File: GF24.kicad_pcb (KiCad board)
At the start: 4 copper layers, 82 x 40 mm, 69 parts, among them J1 Conn_ARM_SWD_TagConnect_TC2030, J2 USB4110GFA, J3 S2B-PH-SM4-TB, J4 0533980671, J5 0533980671, Q1 3904, Q2 DMN3731U-7, Q3 DMN3731U-7, Q4 DMP2004K-7, Q5 DMP2004K-7, Q6 DMP2004K-7, SW2 BOOT, U1 STM32F031C4T6, U2 SAM-M10Q, U3 TPS745, U4 LTC1733, U5 ST-025BH, U6 M24C02-WMN6TP, Y1 CS06465-32M

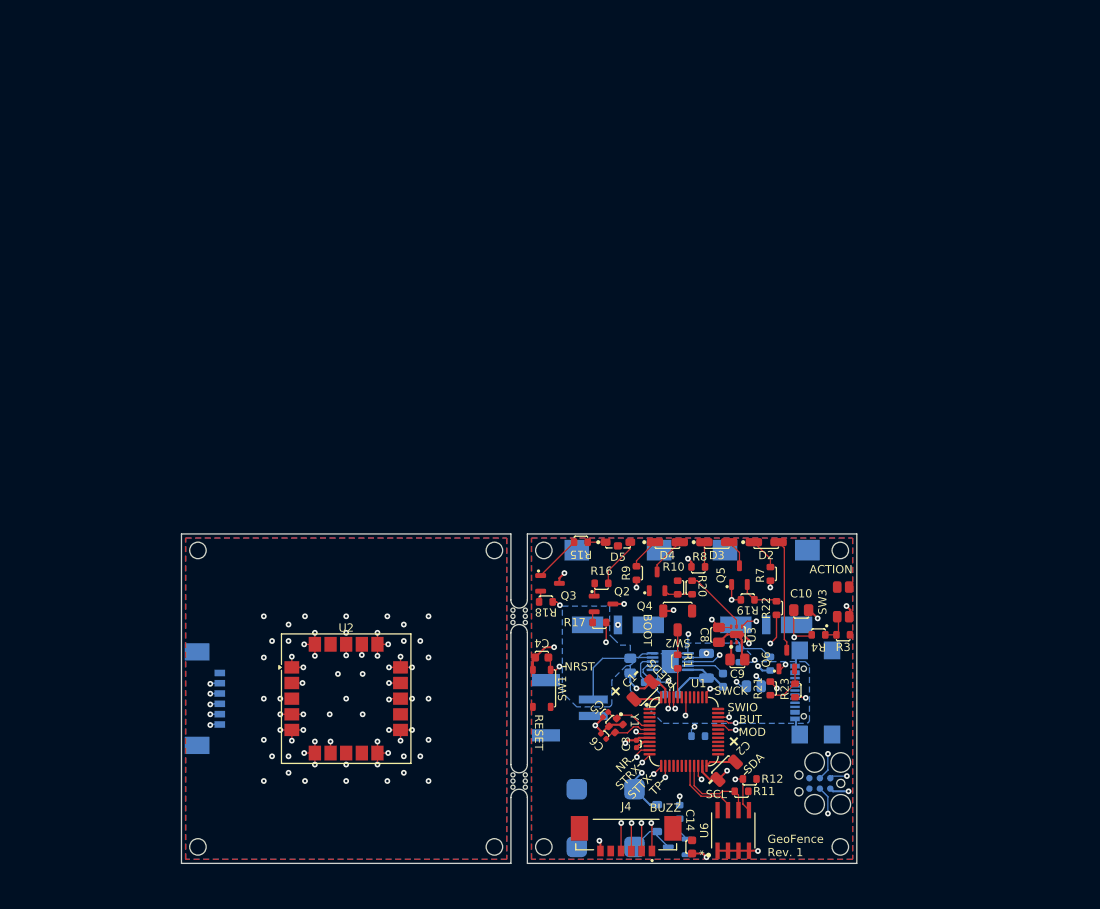
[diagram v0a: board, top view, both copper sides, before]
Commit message: need to finish placement but this is an almost completed R2
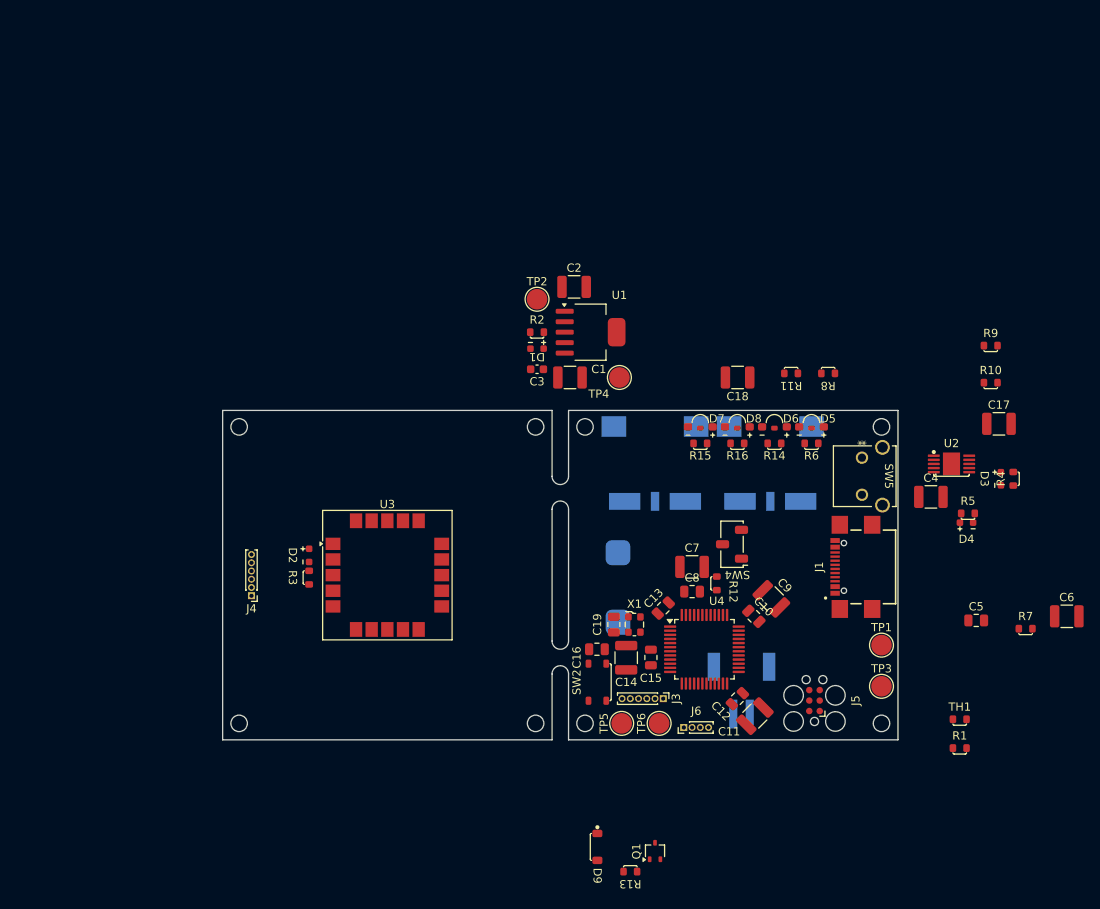
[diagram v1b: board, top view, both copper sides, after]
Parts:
- removed G***: LOGO, MB-Initials:initials-5mm
- removed Q2, Q3: DMN3731U-7, MB-SOT:SOT-23-3
- removed Q4, Q5, Q6: DMP2004K-7, MB-SOT:SOT-23-3
- removed R17, R18, R20, R22, R23: 1k, MB-Generic:R0603_medium
- removed R19, R21: 10k, MB-Generic:R0603_medium
- removed U5: ST-025BH, MB-Buzzer:ST-025BH_SOB
- removed U6: M24C02-WMN6TP, MB-SOIC:SO-8_STM
- removed Y1: CS06465-32M, MB-Crystal:CS06465-32M
- removed mouse-bite-2mm-slot (x2): VAL**, MB-Tab:mouse-bite-2mm-slot
- added BZ1: SMTB-0927-TW-R, MB-Buzzer:SMTB-0927-TW-R, B.Cu at (123.0, 96.5)
- added C16: 100nf, Capacitor_SMD:C_0805_2012Metric, F.Cu at (120.4, 104.0)
- added C17: 1uF, Capacitor_SMD:C_1210_3225Metric, F.Cu at (169.3, 76.6)
- added C18: 1uF, Capacitor_SMD:C_1210_3225Metric, F.Cu at (137.5, 71.0)
- added C19: 100nf, Capacitor_SMD:C_0805_2012Metric, F.Cu at (122.5, 101.0)
- added C7: 10uF, Capacitor_SMD:C_1210_3225Metric, F.Cu at (132.0, 94.0)
- added D6: LED, MB-Opto:WE-1204-Mono-Side, F.Cu at (142.0, 77.0)
- added D7: LED, MB-Opto:WE-1204-Mono-Side, F.Cu at (133.0, 77.0)
- added D8: LED, MB-Opto:WE-1204-Mono-Side, F.Cu at (137.5, 77.0)
- added D9: D, MB-SOD:SOD-123-2, F.Cu at (120.5, 128.0)
- added J6: Conn_01x04_Pin, Connector_PinHeader_1.00mm:PinHeader_1x04_P1.00mm_Vertical, F.Cu at (131.0, 113.5)
- added TP1: TestPoint, TestPoint:TestPoint_Pad_D2.5mm, F.Cu at (155.0, 103.5)
- added TP2: TestPoint, TestPoint:TestPoint_Pad_D2.5mm, F.Cu at (113.2, 61.5)
- added TP3: TestPoint, TestPoint:TestPoint_Pad_D2.5mm, F.Cu at (155.0, 108.5)
- added TP4: TestPoint, TestPoint:TestPoint_Pad_D2.5mm, F.Cu at (123.2, 71.0)
- added TP5: TestPoint, TestPoint:TestPoint_Pad_D2.5mm, F.Cu at (123.5, 113.0)
- added TP6: TestPoint, TestPoint:TestPoint_Pad_D2.5mm, F.Cu at (128.0, 113.0)
- added X1: ECS-2520MV-160-CN, Oscillator:Oscillator_SMD_ECS_2520MV-xxx-xx-4Pin_2.5x2.0mm, F.Cu at (125.0, 101.0)
- C1, C2: value 4.7uF -> 1uF; footprint MB-Generic:C1206_medium -> Capacitor_SMD:C_1210_3225Metric
- C10, C8: value 1uF -> 100nf; footprint MB-Generic:C0805_medium -> Capacitor_SMD:C_0805_2012Metric
- C11: value 4.7uF -> 10uF; footprint MB-Generic:C1206_medium -> Capacitor_SMD:C_1210_3225Metric; moved to F.Cu
- C12: value 0.1uF -> 100nf; footprint MB-Generic:C0603_medium -> Capacitor_SMD:C_0805_2012Metric; moved to F.Cu
- C13, C15: value 1uF -> 100nf; footprint MB-Generic:C0805_medium -> Capacitor_SMD:C_0805_2012Metric; moved to F.Cu
- C14: value 0.1uF -> 1uF; footprint MB-Generic:C0603_medium -> Capacitor_SMD:C_1210_3225Metric
- C3: footprint MB-Generic:C0402_medium -> Capacitor_SMD:C_0603_1608Metric
- C4: value 0.1uF -> 4.7uF; footprint MB-Generic:C0603_medium -> Capacitor_SMD:C_1210_3225Metric
- C5: value 10pF -> 100nf; footprint MB-Generic:C0402_medium -> Capacitor_SMD:C_0805_2012Metric
- C6: value 10pF -> 1uF; footprint MB-Generic:C0402_medium -> Capacitor_SMD:C_1210_3225Metric
- C9: value 1uF -> 10uF; footprint MB-Generic:C0805_medium -> Capacitor_SMD:C_1210_3225Metric
- D1: value D -> LED; footprint MB-SOD:SOD-123-2 -> MB-Opto:WE-0603-Mono-Chip-Advance; moved to F.Cu
- D2, D3, D4: footprint MB-Opto:Kingbright-APDA3020 -> MB-Opto:WE-0603-Mono-Chip-Advance
- D5: value APBDA3020SURKCGKC-GX -> LED; footprint MB-Opto:Kingbright-APBDA3020 -> MB-Opto:WE-1204-Mono-Side
- J1: value Conn_ARM_SWD_TagConnect_TC2030 -> USB4110GFA; footprint MB-Conn:Tag-Connect_TC2030-IDC-FP_2x03_P1.27mm_Vertical -> MB-Conn:GCT_USB4110GFA; moved to F.Cu
- J2: value USB4110GFA -> S2B-PH-SM4-TB; footprint MB-Conn:GCT_USB4110GFA -> MB-Conn:JST_S2B-PH-SM4-TB
- J3: value S2B-PH-SM4-TB -> Conn_01x06_Pin; footprint MB-Conn:JST_S2B-PH-SM4-TB -> Connector_PinHeader_1.00mm:PinHeader_1x06_P1.00mm_Vertical; moved to F.Cu
- J4: value 0533980671 -> Conn_01x06_Pin; footprint MB-Conn:MOLEX_0533980671 -> Connector_PinHeader_1.00mm:PinHeader_1x06_P1.00mm_Vertical
- J5: value 0533980671 -> Conn_ARM_SWD_TagConnect_TC2030; footprint MB-Conn:MOLEX_0533980671 -> Connector:Tag-Connect_TC2030-IDC-FP_2x03_P1.27mm_Vertical; moved to F.Cu
- Q1: footprint MB-SOT:SOT-23-3 -> Package_TO_SOT_SMD:SOT-323_SC-70; moved to F.Cu
- R1: value 10k -> 4.12k
- R11, R12: value 4.7k -> 10k
- R13: value 10k -> 180; moved to F.Cu
- R14: value 1k -> 2; moved to F.Cu
- R15, R16: value 47 -> 2
- R2: value 180 -> 260; moved to F.Cu
- R3: value 1k -> 260
- R4: value 10k -> 1k
- R5: value 1.5k -> 1k; moved to F.Cu
- R6: value 4.12k -> 1k; moved to F.Cu
- R7: value 127 -> 1.5k
- R8: value 127 -> 1k
- R9: value 51 -> 1k
- SW1: footprint MB-SW:PTS815SJM250SMTRLFS -> MB-SW:SW_500ASSP1SM6QE; moved to B.Cu
- SW2: value BOOT -> ~; footprint MB-SW:CJS-1200TA -> MB-SW:PTS815SJM250SMTRLFS
- SW3: footprint MB-SW:TL1016AAF160QG -> MB-SW:SW_500ASSP1SM6QE; moved to B.Cu
- SW4: value ~ -> BOOT; footprint MB-SW:SW_500ASSP1SM6QE -> Button_Switch_SMD:Nidec_Copal_CAS-120A; moved to F.Cu
- SW5: value ~ -> 1-1825027-7; footprint MB-SW:SW_500ASSP1SM6QE -> MB-SW:SW2_1825027-F_TEC; moved to F.Cu
- TH1: moved to F.Cu
- U1: value STM32F031C4T6 -> TPS79533DCQR; footprint MB-STM:LQFP-48_7x7mm_P0.5mm -> Package_TO_SOT_SMD:SOT-223-6
- U2: value SAM-M10Q -> LTC1733; footprint MB-GNSS:SAM-M10Q -> MB-MSOP:10-MSOP-TE
- U3: value TPS745 -> SAM-M10Q; footprint MB-DFN:6-WDFN -> MB-GNSS:SAM-M10Q
- U4: value LTC1733 -> STM32F102C8Tx; footprint MB-MSOP:10-MSOP-TE -> Package_QFP:LQFP-48_7x7mm_P0.5mm; moved to F.Cu
- moved U2 78.8 mm to (163.5, 81.5)
- moved J5 72.9 mm to (146.9, 110.2)
- moved R3 65.2 mm to (85.5, 95.3), turned to -90 degrees
- moved C2 61.6 mm to (117.7, 60.0), turned to 0 degrees
- moved R2 60.8 mm to (113.2, 65.5), turned to 0 degrees
- moved D1 58.8 mm to (113.2, 67.5), turned to 180 degrees
- moved C6 58.1 mm to (177.5, 100.0), turned to 0 degrees
- moved D2 55.5 mm to (85.5, 92.6), turned to -90 degrees
- moved J4 54.7 mm to (78.5, 97.5)
- moved R9 51.1 mm to (168.3, 67.1), turned to 0 degrees
- moved C4 51.1 mm to (161.0, 85.5), turned to 0 degrees
- moved R11 51.1 mm to (144.0, 70.5), turned to 180 degrees
- moved U1 49.8 mm to (119.7, 65.5)
- moved C3 47.1 mm to (113.2, 70.0), turned to 0 degrees
- moved C5 46.4 mm to (166.5, 100.5), turned to 0 degrees
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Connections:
- C10 pad 1: BUTTON -> +3V3
- C11 pad 1: VBUS -> +3V3
- C12 pad 1: /CH-TIMER -> +3V3
- C13 pad 1: BAT+ -> +3V3
- C15 pad 1: MODE -> +3V3
- C2 pad 1: +3V3 -> /REG_I
- C3 pad 1: +3V3 -> Net-(U1-NR)
- C4 pad 1: NRST -> Net-(D3-A)
- C5 pad 1: /OSC-IN -> /CH-TIMER
- C6 pad 1: /OSC-OUT -> Net-(U2-BAT)
- C8 pad 1: /REG_I -> +3V3
- D1 pad 1: +3V3 -> Net-(D1-K)
- D1 pad 2: /BUZZ- -> +3V3
- D2 pad 1: /CHRG_RES -> Net-(D2-K)
- D2 pad 2: /CHRG_QO -> GNSS-3V3
- D3 pad 1: /FAULT_RES -> Net-(D3-K)
- D3 pad 2: /FAULT_QO -> Net-(D3-A)
- D4 pad 1: /PG_RES -> Net-(D4-K)
- D4 pad 2: /PG_QO -> Net-(D3-A)
- D5 pad 1: /STATR_RES -> Net-(D5-K)
- D5 pad 2: +3V3 -> Net-(D3-A)
- J3 pad 2: BAT+ -> /GNSS-ST-TIMEPULSE
- J3 pad 3: unconnected-(J3-Pad3) -> /GNSS-ST-RX2
- J3 pad 4: unconnected-(J3-Pad4) -> /GNSS-ST-TX2
- J4 pad 1: /GNSS-ST-TIMEPULSE -> GNSS-GND
- J4 pad 2: /GNSS-ST-TX -> GNSS-TIMEPULSE
- J4 pad 3: /GNSS-ST-RX -> GNSS-TX
- J4 pad 4: /GNSS-ST-N-RESET -> GNSS-RX
- J4 pad 5: +3V3 -> GNSS-N-RESET
- J4 pad 6: GND -> GNSS-3V3
- J5 pad 1: GNSS-TIMEPULSE -> +3V3
- J5 pad 2: GNSS-TX -> /SWDIO
- J5 pad 3: GNSS-RX -> NRST
- J5 pad 4: GNSS-N-RESET -> /SWDCLK
- J5 pad 5: GNSS-3V3 -> GND
- J5 pad 6: GNSS-GND -> unconnected-(J5-SWO-Pad6)
- R1 pad 1: /BOOT0_RES -> /CH-TH-DIV
- R1 pad 2: /BOOT0 -> Net-(D3-A)
- R10 pad 1: /PG_QG -> /ACT-H
- R10 pad 2: +3V3 -> BUTTON
- R11 pad 1: I2C-SCL -> /MODE-H
- R11 pad 2: +3V3 -> MODE
- R12 pad 1: I2C-SDA -> /BOOT0_RES
- R12 pad 2: +3V3 -> Net-(U4-BOOT0)
- R13 pad 1: /MODE-H -> /BUZZ-QB
- R13 pad 2: MODE -> BUZZER
- R14 pad 1: /MODE-H -> Net-(D6-K)
- R14 pad 2: +3V3 -> GND
- R15 pad 1: /STATR_RES -> Net-(D7-K)
- R15 pad 2: /STATR_QI -> GND
- R16 pad 1: /STATG_QI -> Net-(D8-K)
- R16 pad 2: /STATG_RES -> GND
- R2 pad 1: /BUZZ-QB -> Net-(D1-K)
- R2 pad 2: BUZZER -> GND
- R3 pad 1: /ACT-H -> Net-(D2-K)
- R3 pad 2: +3V3 -> GNSS-GND
- R4 pad 1: /ACT-H -> Net-(D3-K)
- R4 pad 2: BUTTON -> NACPR
- R5 pad 1: GND -> Net-(D4-K)
- R5 pad 2: /CH-PROG -> NFAULT
- R6 pad 1: /CH-TH-DIV -> Net-(D5-K)
- R6 pad 2: VBUS -> NCHRG
- R7 pad 2: /CHRG_RES -> /CH-PROG
- R8 pad 1: GND -> /MODE-H
- R8 pad 2: /FAULT_RES -> +3V3
- R9 pad 1: GND -> /ACT-H
- R9 pad 2: /PG_RES -> +3V3
- SW1 pad 1: unconnected-(SW1-Pad1) -> BAT+
- SW1 pad 2: GND -> /REG_I
- SW1 pad 4: NRST -> unconnected-(SW1-NC-Pad4)
- SW2 pad 1: +3V3 -> unconnected-(SW2-Pad1)
- SW2 pad 2: /BOOT0_RES -> GND
- SW2 pad 3: GND -> unconnected-(SW2-Pad3)
- SW3 pad 1: /ACT-H -> /MODE-H
- SW3 pad 2: unconnected-(SW3-Pad2) -> GND
- SW3 pad 3: GND -> unconnected-(SW3-Pad3)
- SW4 pad 1: BAT+ -> +3V3
- SW4 pad 2: /REG_I -> /BOOT0_RES
- SW4 pad 3: unconnected-(SW4-Pad3) -> GND
- SW5 pad 1: /MODE-H -> /ACT-H
- U1 pad 1: +3V3 -> /REG_I
- U1 pad 2: unconnected-(U1-PC13-Pad2) -> /REG_I
- U1 pad 3: unconnected-(U1-PC14-Pad3) -> GND
- U1 pad 4: unconnected-(U1-PC15-Pad4) -> +3V3
- U1 pad 5: /OSC-IN -> Net-(U1-NR)
- U1 pad 6: /OSC-OUT -> GND
- U2 pad 1: GNSS-GND -> NCHRG
- U2 pad 10: GNSS-GND -> NACPR
- U2 pad 11: GNSS-GND -> GND
- U2 pad 2: GNSS-3V3 -> Net-(D3-A)
- U2 pad 3: unconnected-(U2-V-BCKP-Pad3) -> NFAULT
- U2 pad 4: GNSS-GND -> /CH-TIMER
- U2 pad 5: GNSS-GND -> GND
- U2 pad 6: GNSS-GND -> /CH-TH-DIV
- U2 pad 7: GNSS-TIMEPULSE -> /CH-PROG
- U2 pad 8: unconnected-(U2-SAFEBOOT-N-Pad8) -> Net-(D3-A)
- U2 pad 9: unconnected-(U2-SDA-Pad9) -> Net-(U2-BAT)
- U3 pad 1: +3V3 -> GNSS-GND
- U3 pad 2: unconnected-(U3-NC-Pad2) -> GNSS-3V3
- U3 pad 3: GND -> unconnected-(U3-V-BCKP-Pad3)
- U3 pad 4: /REG_I -> GNSS-GND
- U3 pad 5: PG -> GNSS-GND
- U3 pad 6: /REG_I -> GNSS-GND
- U3 pad 7: GND -> GNSS-TIMEPULSE
- U4 pad 1: N-CHRG -> +3V3
- U4 pad 11: GND -> /GNSS-ST-N-RESET
- U4 pad 2: VBUS -> unconnected-(U4-PC13-Pad2)
- U4 pad 3: N-FAULT -> unconnected-(U4-PC14-Pad3)
- U4 pad 4: /CH-TIMER -> unconnected-(U4-PC15-Pad4)
- U4 pad 5: GND -> Net-(U4-PD0)
- U4 pad 6: /CH-TH-DIV -> unconnected-(U4-PD1-Pad6)
- U4 pad 7: /CH-PROG -> NRST
- U4 pad 8: VBUS -> GND
- U4 pad 9: BAT+ -> +3V3
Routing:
- net GND: track 72.7 -> 0.00 mm, vias 18 -> 0
- net NRST: track 48.6 -> 0.00 mm, vias 3 -> 0
- net GNSS-GND: track 34.2 -> 0.00 mm, vias 62 -> 0
- net GNSS-TX: track 25.5 -> 0.00 mm, vias 2 -> 0
- net GNSS-RX: track 25.4 -> 0.00 mm, vias 2 -> 0
- net /SWDCLK: track 22.4 -> 0.00 mm, vias 2 -> 0
- net N-CHRG: track 22.2 -> 0.00 mm, vias 2 -> 0
- net STATR: track 22.0 -> 0.00 mm, vias 2 -> 0
- net BUTTON: track 21.3 -> 0.00 mm, vias 2 -> 0
- net +3V3: track 21.1 -> 0.00 mm, vias 3 -> 0
- net GNSS-N-RESET: track 20.9 -> 0.00 mm, vias 2 -> 0
- net /SWDIO: track 20.7 -> 0.00 mm, vias 2 -> 0
- net VBUS: track 19.4 -> 0.00 mm, vias 4 -> 0
- net GNSS-TIMEPULSE: track 18.0 -> 0.00 mm, vias 2 -> 0
- net MODE: track 16.6 -> 0.00 mm, vias 3 -> 0
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- removed copper zone on F.Cu, net +3V3
- removed copper zone on In2.Cu, net /REG_I
- removed copper zone on B.Cu, net BAT+
- removed copper zone on B.Cu, net GND
- removed copper zone on In1.Cu, net GNSS-3V3
- removed copper zone on B.Cu, net GNSS-GND
- removed copper zone on F.Cu, net GNSS-GND
- removed copper zone on B.Cu, net VBUS
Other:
- board text removed: "+"
- board text removed: "-"
- board text removed: "ACTION"
- board text removed: "BAT+"
- board text removed: "BOOT"
- board text removed: "BUT"
- board text removed: "BUZZ"
- board text removed: "GeoFence Rev. 1"
- board text removed: "MOD"
- board text removed: "MODE"
- board text removed: "NR"
- board text removed: "NRST"
- board text removed: "PLEDS"
- board text removed: "PWR"
- board text removed: "RESET"
- board text removed: "SCL"
- board text removed: "SDA"
- board text removed: "STRX"
- board text removed: "STTX"
- board text removed: "SWCK"
- board text removed: "SWIO"
- board text removed: "TC"
- board text removed: "TP"
- board text removed: "VBUS"

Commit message: going to make some changes to the I/O
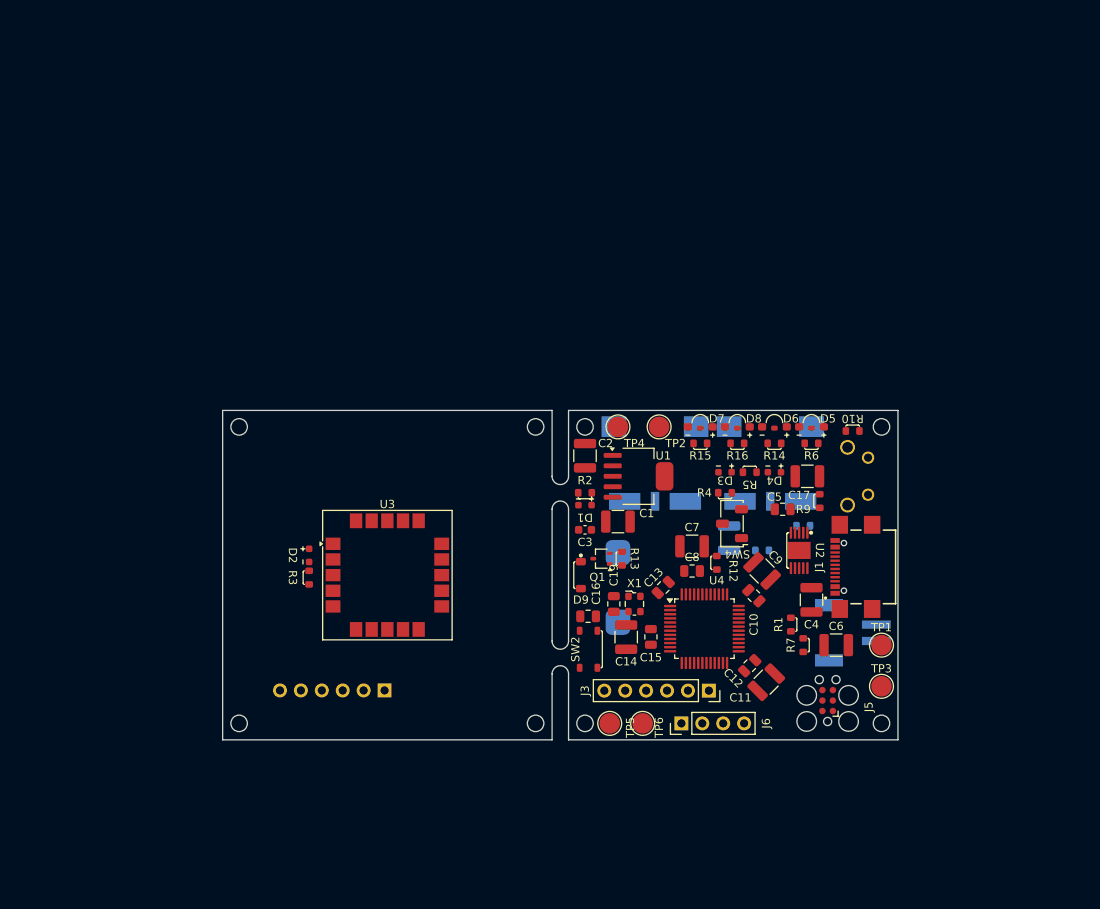
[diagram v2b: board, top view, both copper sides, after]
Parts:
- C18, R11, R8, SW5, TH1: moved to B.Cu
- J3: footprint Connector_PinHeader_1.00mm:PinHeader_1x06_P1.00mm_Vertical -> Connector_PinSocket_2.54mm:PinSocket_1x06_P2.54mm_Vertical
- J4: footprint Connector_PinHeader_1.00mm:PinHeader_1x06_P1.00mm_Vertical -> Connector_PinHeader_2.54mm:PinHeader_1x06_P2.54mm_Vertical; moved to B.Cu
- J6: footprint Connector_PinHeader_1.00mm:PinHeader_1x04_P1.00mm_Vertical -> Connector_PinHeader_2.54mm:PinHeader_1x04_P2.54mm_Vertical
- moved R13 38.0 mm to (123.5, 93.0), turned to -90 degrees
- moved Q1 36.1 mm to (121.0, 93.0), turned to 180 degrees
- moved R4 35.0 mm to (136.0, 85.0), turned to 0 degrees
- moved D3 33.5 mm to (136.0, 82.5), turned to 180 degrees
- moved D9 33.1 mm to (118.5, 95.0)
- moved TH1 31.6 mm to (140.5, 92.0), turned to 180 degrees
- moved C6 28.2 mm to (149.5, 103.5)
- moved R9 28.1 mm to (147.5, 86.0), turned to -90 degrees
- moved C5 27.1 mm to (143.0, 87.0), turned to 180 degrees
- moved R7 27.1 mm to (145.5, 103.5), turned to 90 degrees
- moved R5 27.0 mm to (139.0, 82.5), turned to 180 degrees
- moved R1 25.4 mm to (144.0, 101.0), turned to 90 degrees
- moved C17 24.1 mm to (146.0, 83.0), turned to 180 degrees
- moved D4 24.1 mm to (142.0, 82.5), turned to 180 degrees
- moved R11 21.5 mm to (145.0, 92.0)
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
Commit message: added Wago
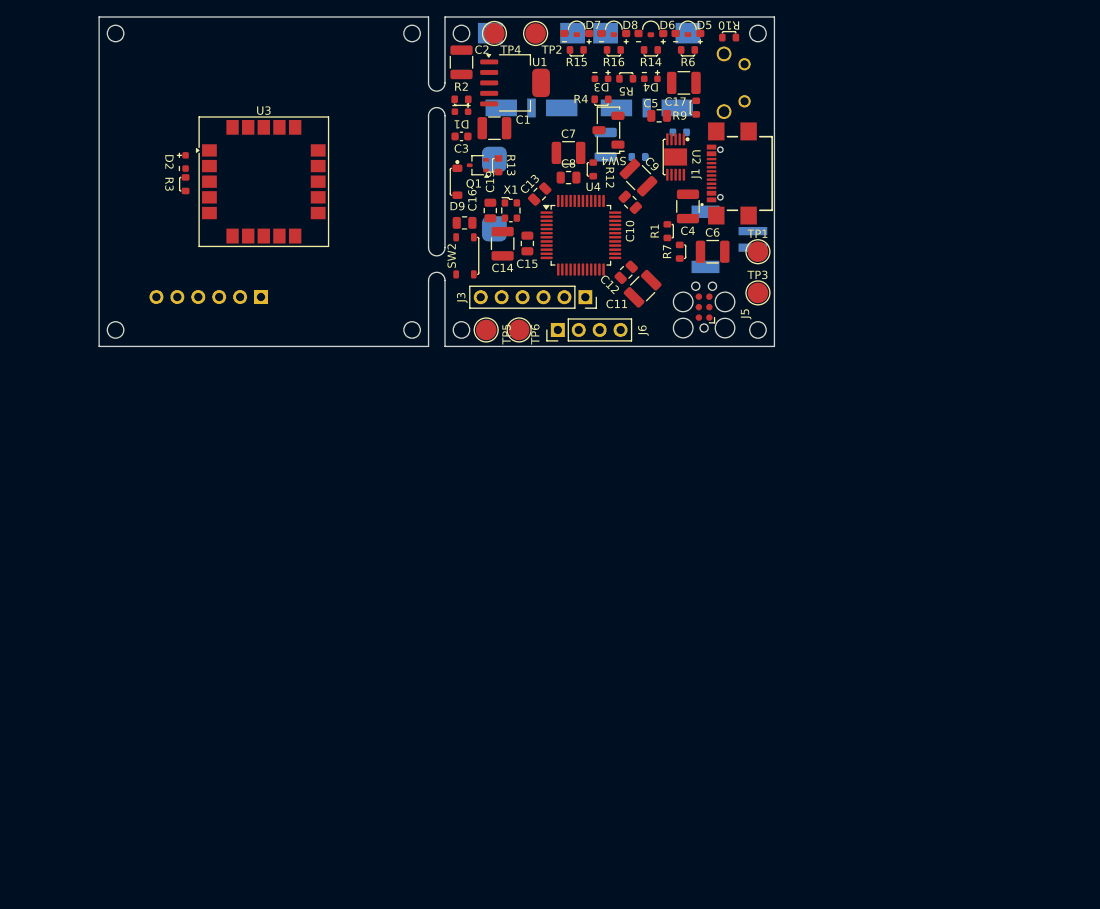
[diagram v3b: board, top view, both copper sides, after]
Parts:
- moved BZ1 50.1 mm to (108.0, 48.7)
- moved C1 50.1 mm to (108.0, 40.7)
- moved C10 50.1 mm to (124.5, 49.7)
- moved C11 50.1 mm to (126.0, 60.2)
- moved C12 50.1 mm to (124.0, 58.2)
- moved C13 50.1 mm to (113.5, 48.7)
- moved C14 50.1 mm to (109.0, 54.8)
- moved C15 50.1 mm to (112.0, 54.7)
- moved C16 50.1 mm to (104.4, 52.2)
- moved C17 50.1 mm to (131.0, 35.2)
- moved C18 50.1 mm to (121.5, 42.7)
- moved C19 50.1 mm to (107.5, 50.7)
- moved C2 50.1 mm to (104.0, 32.7)
- moved C3 50.1 mm to (104.0, 41.7)
- moved C4 50.1 mm to (131.5, 50.2)
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
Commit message: 3D done, started routing
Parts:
- removed J2: S2B-PH-SM4-TB, MB-Conn:JST_S2B-PH-SM4-TB
- removed J5: Conn_ARM_SWD_TagConnect_TC2030, Connector:Tag-Connect_TC2030-IDC-FP_2x03_P1.27mm_Vertical
- removed J6: Conn_01x04_Pin, Connector_PinHeader_2.54mm:PinHeader_1x04_P2.54mm_Vertical
- added BT1: Battery_Cell, MB-SW:Solder_Joint_1_2, F.Cu at (89.1, 87.0)
- BZ1, R11, R8, TH1: moved to F.Cu
- C1, C14, C17, C2, C6: footprint Capacitor_SMD:C_1210_3225Metric -> Capacitor_SMD:C_0603_1608Metric
- C11, C4, C7, C9: footprint Capacitor_SMD:C_1210_3225Metric -> Capacitor_SMD:C_0805_2012Metric
- C18: footprint Capacitor_SMD:C_1210_3225Metric -> Capacitor_SMD:C_0603_1608Metric; moved to F.Cu
- D2, D5, D6, D7, D8, R14, R15, R16, R3, R6, U3: moved to B.Cu
- J3: value Conn_01x06_Pin -> Conn_ARM_SWD_TagConnect_TC2030; footprint Connector_PinSocket_2.54mm:PinSocket_1x06_P2.54mm_Vertical -> Connector:Tag-Connect_TC2030-IDC-FP_2x03_P1.27mm_Vertical; moved to B.Cu
- J4: value Conn_01x06_Pin -> Conn_01x04_Pin; footprint Connector_PinHeader_2.54mm:PinHeader_1x06_P2.54mm_Vertical -> Connector_PinHeader_2.54mm:PinHeader_1x04_P2.54mm_Horizontal; moved to F.Cu
- SW1: value ~ -> EG1205; footprint MB-SW:SW_500ASSP1SM6QE -> MB-SW:Solder_Joint_1_2; moved to F.Cu
- SW3: value ~ -> BOOT; footprint MB-SW:SW_500ASSP1SM6QE -> Button_Switch_SMD:Nidec_Copal_CAS-120A; moved to F.Cu
- SW4: value BOOT -> EG1205; footprint Button_Switch_SMD:Nidec_Copal_CAS-120A -> MB-SW:Solder_Joint_1_2
- SW5: value 1-1825027-7 -> 360-2674-ND; footprint MB-SW:SW2_1825027-F_TEC -> MB-SW:Solder_Joint_1_2; moved to F.Cu
- TP1, TP2, TP3, TP4: footprint TestPoint:TestPoint_Pad_D2.5mm -> TestPoint:TestPoint_Pad_D1.5mm
- TP5, TP6: footprint TestPoint:TestPoint_Pad_D2.5mm -> TestPoint:TestPoint_Pad_D1.5mm; moved to B.Cu
- moved SW5 89.0 mm to (52.0, 54.4), turned to 0 degrees
- moved R10 85.3 mm to (54.5, 53.2), turned to 90 degrees
- moved R9 82.3 mm to (52.0, 55.5), turned to 0 degrees
- moved SW3 80.5 mm to (53.0, 66.5)
- moved C17 77.4 mm to (55.2, 51.0)
- moved R13 70.9 mm to (52.0, 88.0), turned to 90 degrees
- moved Q1 70.7 mm to (53.0, 92.0), turned to 0 degrees
- moved SW4 70.1 mm to (54.4, 60.0), turned to 90 degrees
- moved R12 66.8 mm to (56.0, 64.8), turned to 90 degrees
- moved D9 63.5 mm to (59.0, 92.5), turned to 180 degrees
- moved U1 62.8 mm to (78.0, 89.0), turned to 180 degrees
- moved D1 62.8 mm to (58.0, 81.5), turned to 0 degrees
- moved SW1 61.9 mm to (89.0, 91.0), turned to -90 degrees
- moved R2 61.7 mm to (61.0, 81.5)
- moved C2 59.7 mm to (85.5, 89.5)
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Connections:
- net Net-(D3-A) renamed /USBC+
- net Net-(U1-NR) renamed /Noise_Reduction
- net Net-(U4-BOOT0) renamed /BOOT0_I
- net Net-(U4-PD0) renamed /CLK_OUT
- C6 pad 1: Net-(U2-BAT) -> BAT+
- D2 pad 2: GNSS-3V3 -> +3V3
- J3 pad 1: GND -> +3V3
- J3 pad 2: /GNSS-ST-TIMEPULSE -> /SWDIO
- J3 pad 3: /GNSS-ST-RX2 -> NRST
- J3 pad 4: /GNSS-ST-TX2 -> /SWDCLK
- J3 pad 5: /GNSS-ST-N-RESET -> GND
- J3 pad 6: +3V3 -> unconnected-(J3-SWO-Pad6)
- J4 pad 1: GNSS-GND -> +3V3
- J4 pad 2: GNSS-TIMEPULSE -> /DEBUG_ST_TX
- J4 pad 3: GNSS-TX -> /DEBUG_ST_RX
- J4 pad 4: GNSS-RX -> GND
- R3 pad 2: GNSS-GND -> GND
- SW3 pad 1: /MODE-H -> +3V3
- SW3 pad 2: GND -> /BOOT0_RES
- SW3 pad 3: unconnected-(SW3-Pad3) -> GND
- SW4 pad 1: +3V3 -> /MODE-H
- SW4 pad 2: /BOOT0_RES -> GND
- TP3 pad 1: Net-(U2-BAT) -> BAT+
- TP5 pad 1: /GNSS-ST-TX2 -> GNSS-RX
- TP6 pad 1: /GNSS-ST-RX2 -> GNSS-TX
- U2 pad 9: Net-(U2-BAT) -> BAT+
- U3 pad 1: GNSS-GND -> GND
- U3 pad 10: GNSS-GND -> GND
- U3 pad 11: GNSS-GND -> GND
- U3 pad 15: GNSS-GND -> GND
- U3 pad 16: GNSS-GND -> GND
- U3 pad 17: GNSS-3V3 -> +3V3
- U3 pad 2: GNSS-3V3 -> +3V3
- U3 pad 20: GNSS-GND -> GND
- U3 pad 4: GNSS-GND -> GND
- U3 pad 5: GNSS-GND -> GND
- U3 pad 6: GNSS-GND -> GND
- U4 pad 11: /GNSS-ST-N-RESET -> GNSS-N-RESET
- U4 pad 12: /GNSS-ST-TX2 -> GNSS-RX
- U4 pad 13: /GNSS-ST-RX2 -> GNSS-TX
- U4 pad 14: /GNSS-ST-TIMEPULSE -> GNSS-TIMEPULSE
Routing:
- net GND: track 0.00 -> 81.2 mm, vias 0 -> 7
- net /USBC+: track 0.00 -> 52.3 mm
- net +3V3: track 0.00 -> 37.6 mm, vias 0 -> 1
- net BUTTON: track 0.00 -> 32.5 mm
- net BUZZER: track 0.00 -> 30.9 mm
- net STATG: track 0.00 -> 21.4 mm, vias 0 -> 1
- net /BOOT0_I: track 0.00 -> 20.0 mm
- net STATR: track 0.00 -> 19.0 mm, vias 0 -> 1
- net STATGPS: track 0.00 -> 17.8 mm, vias 0 -> 1
- net NRST: track 0.00 -> 15.6 mm, vias 0 -> 2
- net GNSS-N-RESET: track 0.00 -> 12.4 mm, vias 0 -> 1
- net /BUZZ-: track 0.00 -> 10.2 mm
- net NCHRG: track 0.00 -> 9.16 mm, vias 0 -> 1
- net NFAULT: track 0.00 -> 9.06 mm, vias 0 -> 2
- net /CH-TH-DIV: track 0.00 -> 7.76 mm
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- added copper zone on F.Cu, net +3V3
- added copper zone on F.Cu, net /REG_I
- added copper zone on F.Cu, net BAT+
- added copper zone on B.Cu, net GND
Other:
- board size 82 x 40 mm -> 44 x 44 mm
- board text added: "3 degree taper 17mm lid height 0.89093mm loss per side: should be close to 43mm^2 footprint near very top but model says more than 44"
- board text added: "BATTERY H:7.1mm"
- board text added: "Mounting Point Height: 5mm Battery Height: 7.1mm Should need at least 2.5mm standoffs"

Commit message: finished routing for Rev 2
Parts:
- added G***: LOGO, MB-Initials:initials-5mm, B.Cu at (63.1, 90.6)
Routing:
- net GND: track 81.2 -> 143.7 mm, vias 7 -> 19
- net NRST: track 15.6 -> 46.9 mm, vias 2 -> 4
- net /SWDCLK: track 0.00 -> 29.6 mm, vias 0 -> 2
- net /SWDIO: track 0.00 -> 28.8 mm, vias 0 -> 2
- net +3V3: track 37.6 -> 65.4 mm, vias 1 -> 5
- net /MODE-H: track 0.00 -> 26.1 mm, vias 0 -> 1
- net BAT+: track 6.08 -> 28.9 mm, vias 0 -> 2
- net /DEBUG_ST_TX: track 0.00 -> 19.6 mm, vias 0 -> 1
- net /USBC+: track 52.3 -> 71.5 mm, vias 0 -> 3
- net /DEBUG_ST_RX: track 0.00 -> 18.8 mm, vias 0 -> 1
- net GNSS-TX: track 0.00 -> 16.0 mm, vias 0 -> 1
- net MODE: track 3.92 -> 19.4 mm, vias 0 -> 2
- net GNSS-RX: track 0.00 -> 13.8 mm, vias 0 -> 1
- net /ACT-H: track 3.18 -> 9.90 mm, vias 0 -> 2
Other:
- board text added: "GF24 Rev. 2"
